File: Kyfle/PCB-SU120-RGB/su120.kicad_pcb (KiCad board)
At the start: 2 copper layers, 124.8 x 95.9 mm, 173 parts, among them J1 MJ-4PP-9, J2 Conn_01x03, J3 Conn_01x08, J4 Conn_01x08, J6 MJ-4PP-9, SW1 SW_PUSH_LED, SW10 SW_PUSH_LED, SW11 SW_PUSH_LED, SW12 SW_PUSH_LED, SW13 SW_PUSH_LED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

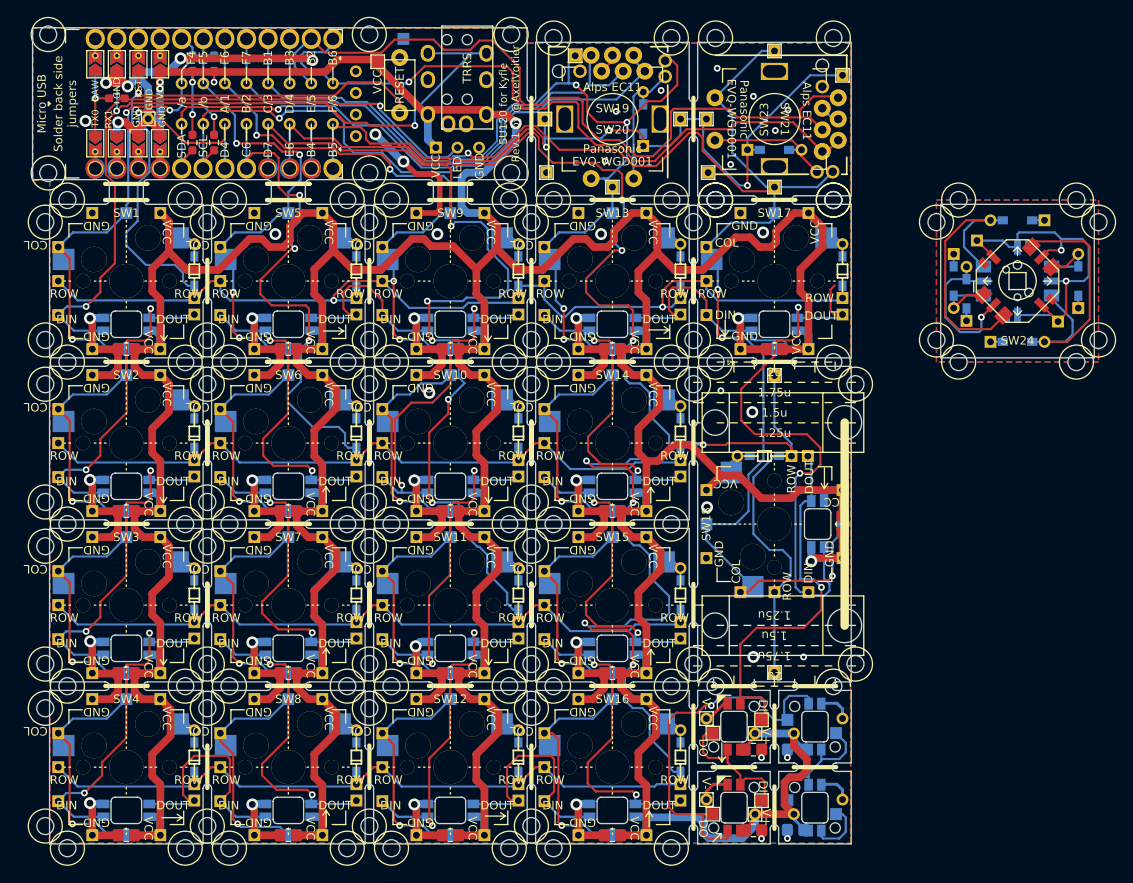
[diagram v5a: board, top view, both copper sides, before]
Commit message: Yet another big update
- Integrated 5-way switch (instead of one of the encoder)
- Based on corrected footprint for roller encoder, it has been repositioned
- Touching up lots of silk
- 2u board made as a footprint module as well
- Fixed a potential short with 2u stabiliser metal bar on VCC and GND
- Added various 3d models
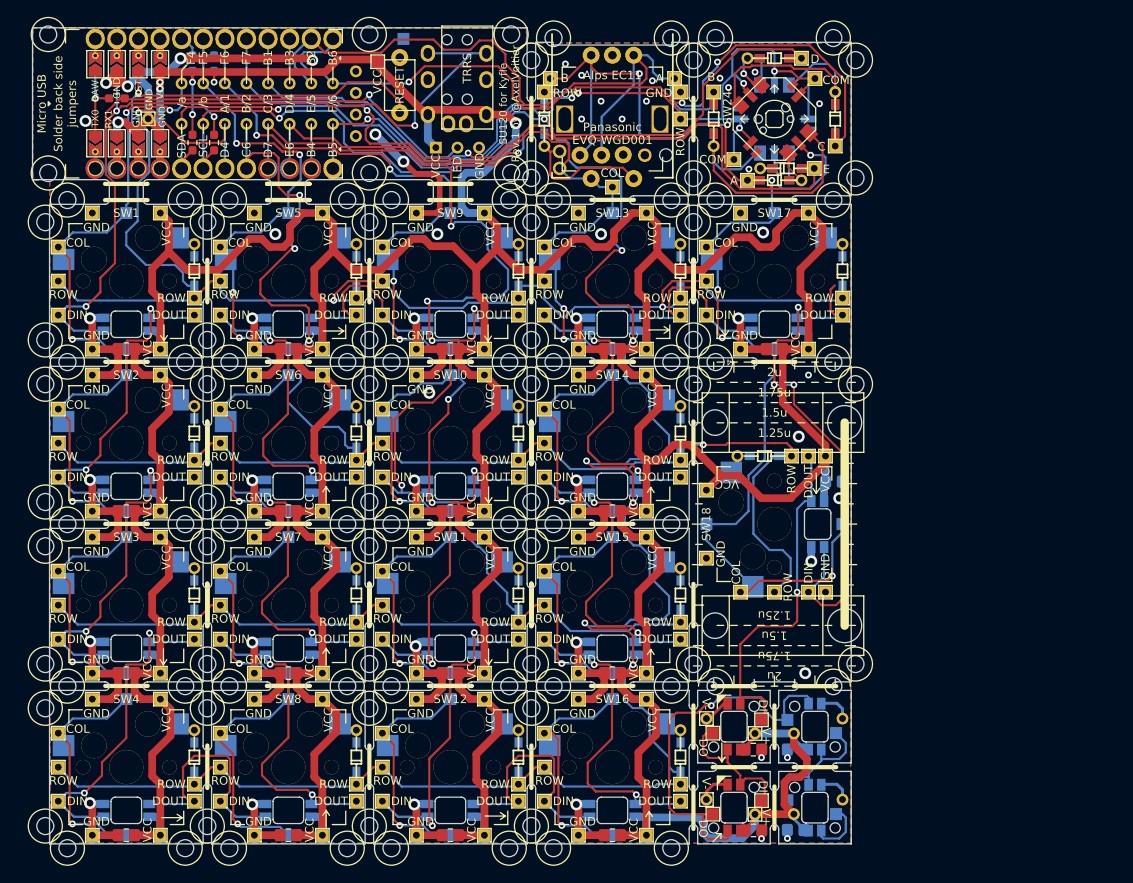
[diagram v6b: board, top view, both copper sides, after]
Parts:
- removed the %R at (127.8, 85.7) (x3)
- removed the %R at (156.4, 85.7) (x4)
- removed the %R at (108.7, 66.7)
- removed the ? at (137.3, 97.9)
- removed the ? at (118.3, 97.9)
- removed the ? at (127.8, 66.7)
- removed the ? at (106.5, 66.7)
- removed the ? at (108.7, 66.7)
- removed the ? at (127.8, 64.0)
- removed the ? at (137.3, 130.7)
- removed the ? at (118.3, 130.7)
- removed D19: D, Kyfle Footprints:diode_TH_SMD_rev3
- removed H133, H134, H136, H137, H139, H140, H171, H46, H50: MountingHole_Pad, Kyfle Footprints:1pin_rect_conn
- removed Ref** (x2): Val**, Kyfle Footprints:M2_Hole_Standoff_Default_Cleareance_Half_Silk
- removed SW21: Rotary_Encoder_Switch, Kyfle Footprints:RotaryEncoder_Alps_EC11E-Switch_Vertical_H20mm_rev2
- removed SW23: Rotary_Encoder_Switch, Kyfle Footprints:RollerEncoder_Panasonic_EVQWGD001_No_Cutout
- added %R (x2): SW_Push, Kyfle Footprints:CherryMX_Kyfle_v1_Module_2_M2, F.Cu at (108.7, 66.7)
- added %R (x2): SW_Push, Kyfle Footprints:CherryMX_Kyfle_v1_Module_2_M2, F.Cu at (127.8, 66.7)
- added H101: MountingHole_Pad, Kyfle Footprints:1pin_rect_conn, F.Cu at (116.0, 61.9)
- added H102: MountingHole_Pad, Kyfle Footprints:1pin_rect_conn, F.Cu at (101.4, 61.9)
- D1, D2, D3, D4, D5: footprint Kyfle Footprints:diode_TH_SMD_rev3 -> Kyfle Footprints:diode_TH_SMD_rev3_alt
- H135, H138, H170: moved to F.Cu
- SW1, SW10, SW11, SW12, SW13, SW14, SW15, SW16, SW2, SW3, SW4, SW5, SW6, SW7, SW8, SW9: footprint Kyfle Footprints:CherryMX_Kyfle_v1_Module -> Kyfle Footprints:CherryMX_Kyfle_v1_Module_1u
- SW17: footprint Kyfle Footprints:CherryMX_Kyfle_v1_Module_For_Rotated -> Kyfle Footprints:CherryMX_Kyfle_v1_Module_1u
- SW18: footprint Kyfle Footprints:CherryMX_Kyfle_v1_Module_For_Rotated -> Kyfle Footprints:CherryMX_Kyfle_v1_Module_2u
- moved D5 44.3 mm to (127.8, 59.5), turned to 0 degrees
- moved H6 40.4 mm to (132.6, 61.9), turned to 90 degrees
- moved D3 37.7 mm to (120.7, 66.7), turned to 90 degrees
- moved SW24 34.3 mm to (127.8, 66.7), turned to 135 degrees
- moved SW24 34.3 mm to (127.8, 66.7), turned to 90 degrees
- moved D4 33.8 mm to (134.9, 66.7), turned to 270 degrees
- moved H6 30.1 mm to (123.0, 71.4), turned to 90 degrees
- moved D2 25.7 mm to (129.3, 72.5), turned to 0 degrees
- moved D1 24.2 mm to (127.8, 73.9), turned to 180 degrees
- moved H170 18.4 mm to (116.7, 63.5)
- moved D18 11.6 mm to (100.7, 66.7), turned to 270 degrees
- moved SW19 1.60 mm to (108.7, 65.1), turned to 90 degrees
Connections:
- D1 pad 1: Y1 -> Net-(D1-Pad1)
- D1 pad 2: Net-(D1-Pad2) -> X7
- D2 pad 1: Y6 -> Net-(D2-Pad1)
- D2 pad 2: Net-(D2-Pad2) -> X5
- D3 pad 1: Y2 -> Net-(D3-Pad1)
- D3 pad 2: Net-(D3-Pad2) -> X8
- D4 pad 1: Y3 -> Net-(D4-Pad1)
- D4 pad 2: Net-(D4-Pad2) -> X9
- D5 pad 1: Y4 -> Net-(D5-Pad1)
- D5 pad 2: Net-(D5-Pad2) -> X10
- H6 pad 1: X5 -> Y6 (x2)
- SW19 pad A: X10 -> X7
- SW19 pad B: X9 -> X8
- SW20 pad A: X10 -> X8
- SW20 pad B: X9 -> X7
- SW24 pad A: Net-(D1-Pad2) -> Net-(D1-Pad1) (x2)
- SW24 pad B: Net-(D3-Pad2) -> Net-(D3-Pad1) (x2)
- SW24 pad C: Net-(D4-Pad2) -> Net-(D4-Pad1) (x2)
- SW24 pad Com: X5 -> Y6 (x2)
- SW24 pad D: Net-(D5-Pad2) -> Net-(D5-Pad1) (x2)
- SW24 pad E: Net-(D2-Pad2) -> Net-(D2-Pad1) (x2)
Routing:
- net X5: track 240.1 -> 177.3 mm, vias 6 -> 5
- net X9: track 75.1 -> 116.5 mm, vias 1 -> 4
- net Net-(D3-Pad1): track 0.00 -> 35.2 mm
- net Net-(D3-Pad2): track 33.6 -> 0.00 mm
- net Net-(D4-Pad2): track 33.1 -> 0.00 mm
- net Net-(D4-Pad1): track 0.00 -> 30.5 mm
- net X4: track 217.1 -> 190.9 mm, vias 7 -> 6
- net X10: track 74.8 -> 99.7 mm, vias 1 -> 2
- net Y2: track 205.0 -> 183.8 mm
- net Net-(D2-Pad1): track 0.00 -> 19.3 mm, vias 0 -> 1
- net Net-(D2-Pad2): track 18.7 -> 0.00 mm, vias 1 -> 0
- net Net-(D19-Pad2): track 15.4 -> 0.00 mm
- net VCC: track 745.3 -> 759.3 mm
- net GND: track 303.0 -> 291.3 mm, vias 48 -> 51
- net Net-(D5-Pad1): track 0.00 -> 10.7 mm, vias 0 -> 1
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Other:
- board size 124.8 x 95.9 mm -> 96.2 x 95.9 mm
- board text added: "C"
- board text added: "COM"
- board text added: "D"
- board text added: "E"

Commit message: PCB: Adding mouse bites to break away tabs
And increasing tabs width from 4mm to 5mm.
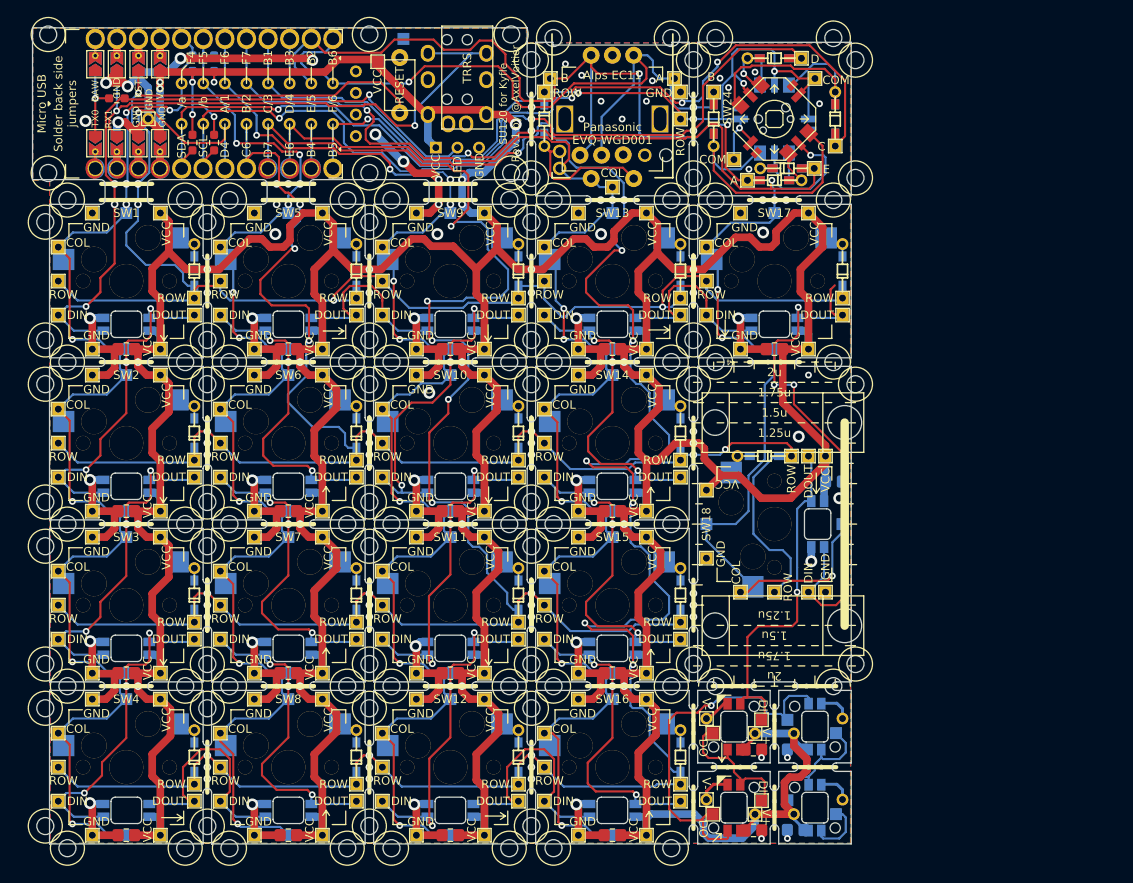
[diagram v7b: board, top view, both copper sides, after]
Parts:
- REF**: footprint Kyfle Footprints:Slot_Cross_2.9mm_7.525mm -> Kyfle Footprints:Slot_Cross_2.9mm_7.025mm
- REF** (x12): footprint Kyfle Footprints:Slot_Half_Line_1mm_7.525mm -> Kyfle Footprints:Slot_Half_Line_1mm_7.025mm
- REF** (x11): footprint Kyfle Footprints:Slot_Cross_1mm_7.525mm -> Kyfle Footprints:Slot_Cross_1mm_7.025mm
- REF**: footprint Kyfle Footprints:Slot_Half_Line_2.9mm_7.525mm -> Kyfle Footprints:Slot_Half_Line_2.9mm_7.025mm
- REF** (x2): footprint Kyfle Footprints:Slot_Tee_2.9mm_7.525mm -> Kyfle Footprints:Slot_Tee_2.9mm_7.025mm
- REF**: footprint Kyfle Footprints:Slot_Tee_1mm_7.525mm -> Kyfle Footprints:Slot_Tee_1mm_7.025mm
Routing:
- net Y3: track 193.0 -> 204.8 mm, vias 5 -> 8
- net Y2: track 183.8 -> 192.4 mm, vias 4 -> 9
- net Y4: track 254.4 -> 260.3 mm, vias 7 -> 11
- net GND: track 291.3 -> 288.9 mm, vias 51 -> 110
- net X3: track 167.6 -> 169.9 mm, vias 7 -> 9
- net Y1: track 166.0 -> 168.3 mm, vias 3 -> 5
- net X2: track 155.4 -> 157.2 mm, vias 7 -> 9
- net X1: track 156.2 -> 158.0 mm, vias 6 -> 8
- net X4: track 190.9 -> 192.2 mm, vias 6 -> 7
- net X9: track 116.5 -> 115.2 mm
- net Net-(H154-Pad1): track 41.3 -> 40.3 mm
- net X7: track 101.1 -> 100.4 mm
- net X5: track 177.3 -> 176.6 mm, vias 5 -> 7
- net VCC: track 759.3 -> 758.6 mm, vias 7 -> 31
- net Net-(SW4-Pad2): track 28.0 -> 28.7 mm
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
